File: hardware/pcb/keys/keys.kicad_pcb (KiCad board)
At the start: 2 copper layers, 2 x 2 mm, 28 parts, among them J1 Conn_02x08_Odd_Even, J2 Conn_02x08_Odd_Even, SW1 SW_SPST, SW11 SW_SPST, SW12 SW_SPST, SW17 SW_SPST, SW18 SW_SPST, SW2 SW_SPST, SW23 SW_SPST, SW24 SW_SPST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

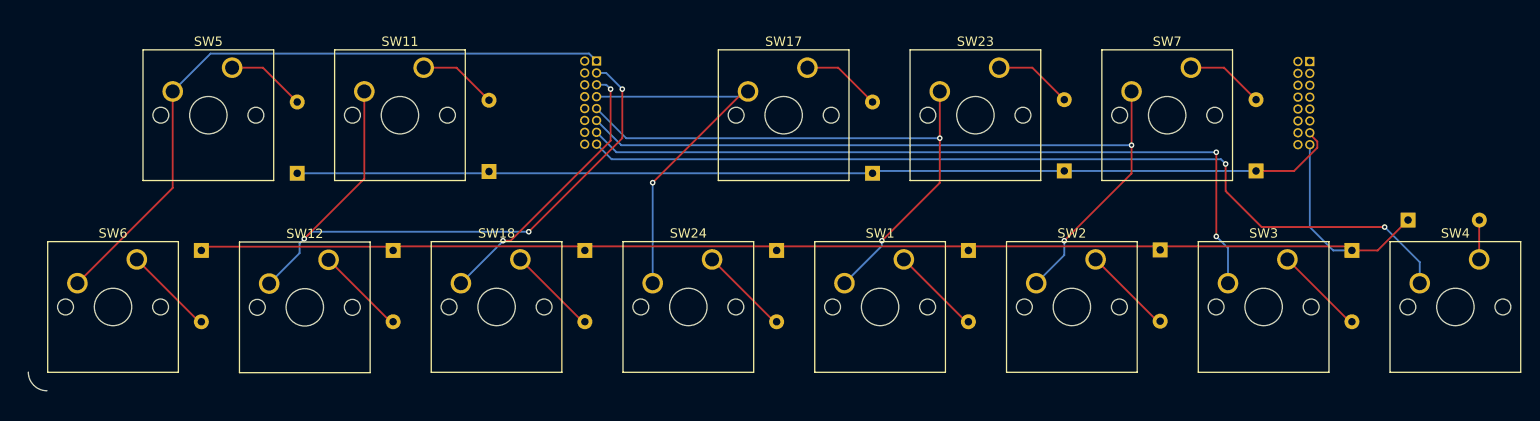
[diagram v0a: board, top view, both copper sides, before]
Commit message: hardware: add schematics
add controls, io, keys, and nucleo hat boards
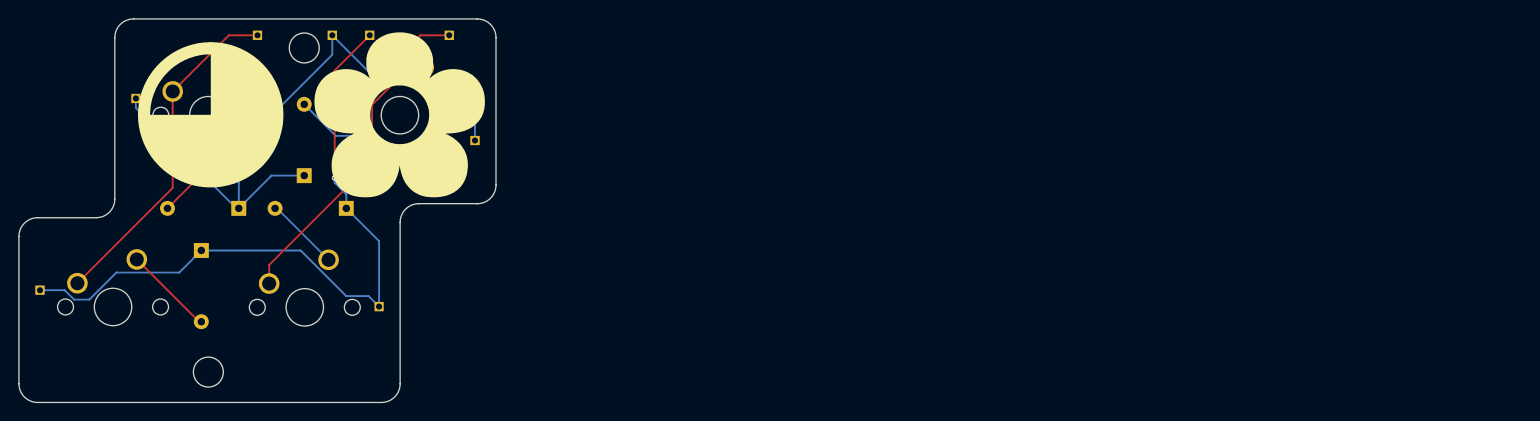
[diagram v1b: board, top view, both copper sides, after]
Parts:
- removed D1, D17, D18, D2, D23, D24, D3, D4, D7: D, Diode_THT:D_DO-35_SOD27_P7.62mm_Horizontal
- removed J1, J2: Conn_02x08_Odd_Even, Connector_PinHeader_1.27mm:PinHeader_2x08_P1.27mm_Vertical
- removed SW1, SW17, SW18, SW2, SW23, SW24, SW3, SW4, SW7: SW_SPST, Button_Switch_Keyboard:SW_Cherry_MX_1.00u_PCB
- added COL: Conn_01x01, Connector_PinHeader_1.27mm:PinHeader_1x01_P1.27mm_Vertical, B.Cu at (99.0, 56.5)
- added COL: Conn_01x01, Connector_PinHeader_1.27mm:PinHeader_1x01_P1.27mm_Vertical, B.Cu at (119.5, 56.5)
- added G***: LOGO, keys:circle, F.Cu at (94.0, 65.0)
- added G***: LOGO, keys:flower, F.Cu at (114.2, 65.0)
- added J5: Conn_01x01, Connector_PinHeader_1.27mm:PinHeader_1x01_P1.27mm_Vertical, B.Cu at (86.0, 63.2)
- added J6: Conn_01x01, Connector_PinHeader_1.27mm:PinHeader_1x01_P1.27mm_Vertical, B.Cu at (75.8, 83.8)
- added J7: Conn_01x01, Connector_PinHeader_1.27mm:PinHeader_1x01_P1.27mm_Vertical, B.Cu at (122.2, 67.8)
- added J8: Conn_01x01, Connector_PinHeader_1.27mm:PinHeader_1x01_P1.27mm_Vertical, B.Cu at (112.0, 85.5)
- added ROW1: Conn_01x01, Connector_PinHeader_1.27mm:PinHeader_1x01_P1.27mm_Vertical, B.Cu at (107.0, 56.5)
- added ROW2: Conn_01x01, Connector_PinHeader_1.27mm:PinHeader_1x01_P1.27mm_Vertical, B.Cu at (111.0, 56.5)
- moved D11 19.8 mm to (104.0, 71.5)
- moved D5 7.29 mm to (97.0, 75.0), turned to 180 degrees
- moved D12 6.73 mm to (108.5, 75.0), turned to 180 degrees
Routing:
- net I8: track 97.2 -> 0.00 mm, vias 2 -> 0
- net I6: track 83.0 -> 0.00 mm, vias 2 -> 0
- net I7: track 81.7 -> 0.00 mm, vias 2 -> 0
- net O8: track 146.8 -> 75.1 mm, vias 0 -> 1
- net I5: track 62.7 -> 0.00 mm, vias 2 -> 0
- net O7: track 112.1 -> 68.9 mm
- net I4: track 41.4 -> 0.00 mm, vias 1 -> 0
- net I1: track 72.0 -> 36.3 mm
- net I2: track 71.9 -> 36.3 mm, vias 3 -> 0
- net I3: track 29.5 -> 0.00 mm, vias 2 -> 0
- net Net-(D11-A): track 8.42 -> 19.1 mm, vias 0 -> 1
- net Net-(D3-A): track 9.66 -> 0.00 mm
- net Net-(D24-A): track 9.66 -> 0.00 mm
- net Net-(D18-A): track 9.66 -> 0.00 mm
- net Net-(D1-A): track 9.66 -> 0.00 mm
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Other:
- board size 2 x 2 mm -> 51 x 41 mm
